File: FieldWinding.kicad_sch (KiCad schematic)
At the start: 39 parts, among them J9 Conn_02x10_Odd_Even, U27 ADM3485, U29 ADM3485, U30 ADM3485, U67 ADM3485, U72 LMV321

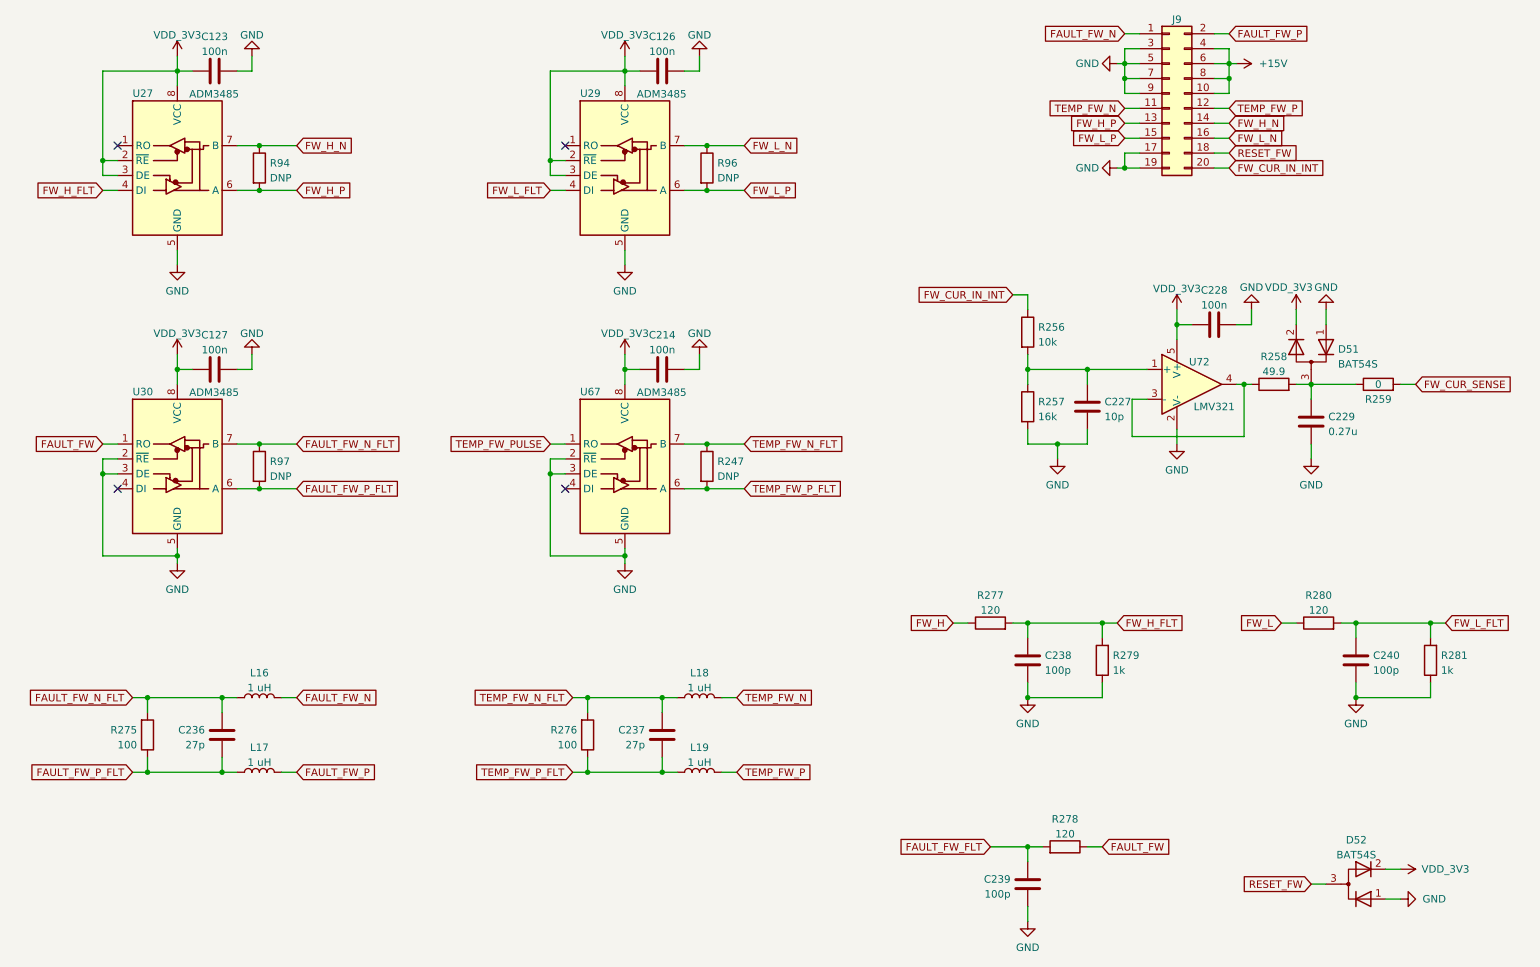
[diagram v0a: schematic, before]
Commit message: Изменения в схеме: убрал разъемы датчиков тока
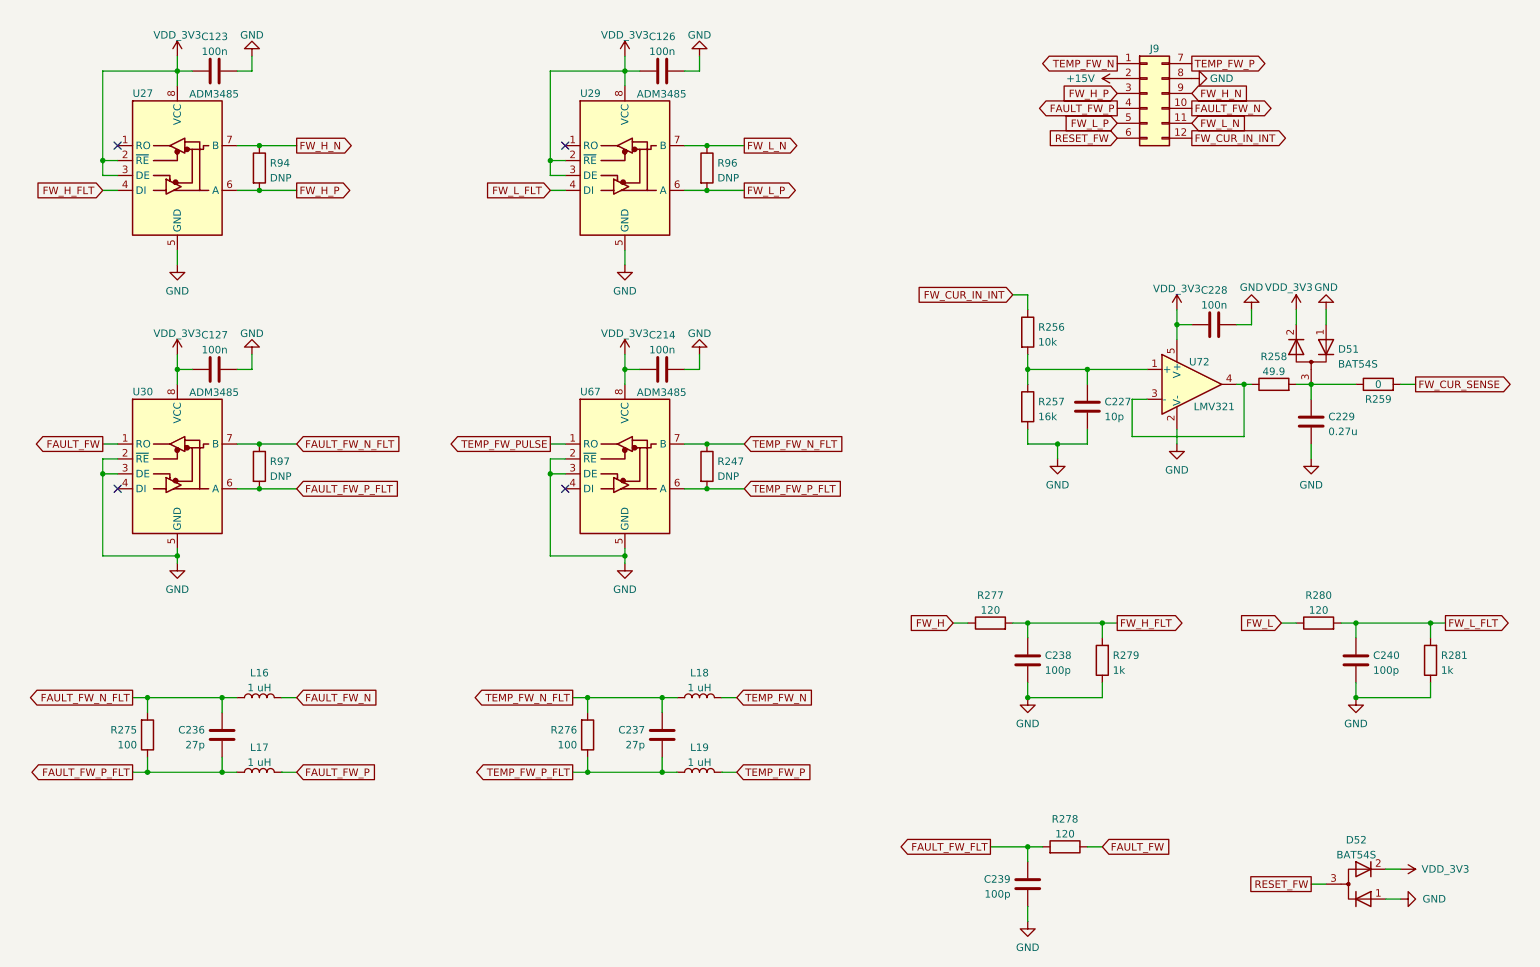
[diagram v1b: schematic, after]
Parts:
- removed J9: Conn_02x10_Odd_Even, Project_Library:2-338069-0, symbol Connector_Generic:Conn_02x10_Odd_Even
- added J9: ~, Connector_Molex:Molex_Micro-Fit_3.0_43045-1200_2x06_P3.00mm_Horizontal, symbol Connector_Generic:Conn_02x06_Top_Bottom
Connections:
- net +15V: now also J9.2 (Pin_2)
- net FAULT_FW_N: now also J9.10 (Pin_10)
- net FAULT_FW_P: now also J9.4 (Pin_4)
- net FW_CUR_IN_INT: now also J9.12 (Pin_12)
- net FW_H_N: now also J9.9 (Pin_9)
- net FW_H_P: now also J9.3 (Pin_3)
- net FW_L_N: now also J9.11 (Pin_11)
- net FW_L_P: now also J9.5 (Pin_5)
- net GND: now also J9.8 (Pin_8)
- net RESET_FW: now also J9.6 (Pin_6)
- net TEMP_FW_N: now also J9.1 (Pin_1)
- net TEMP_FW_P: now also J9.7 (Pin_7)

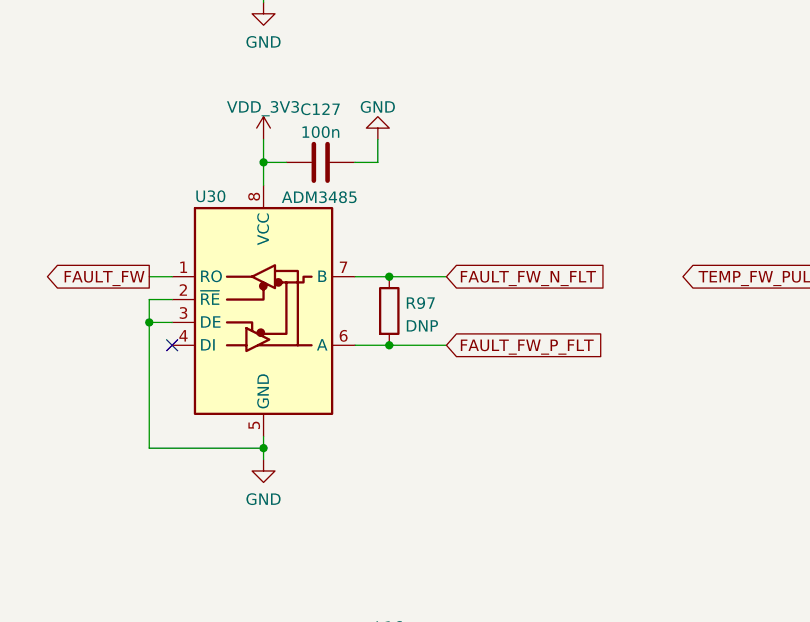
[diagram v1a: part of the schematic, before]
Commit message: Изменения: добавил 3или для фолтов трёхфазного модуля
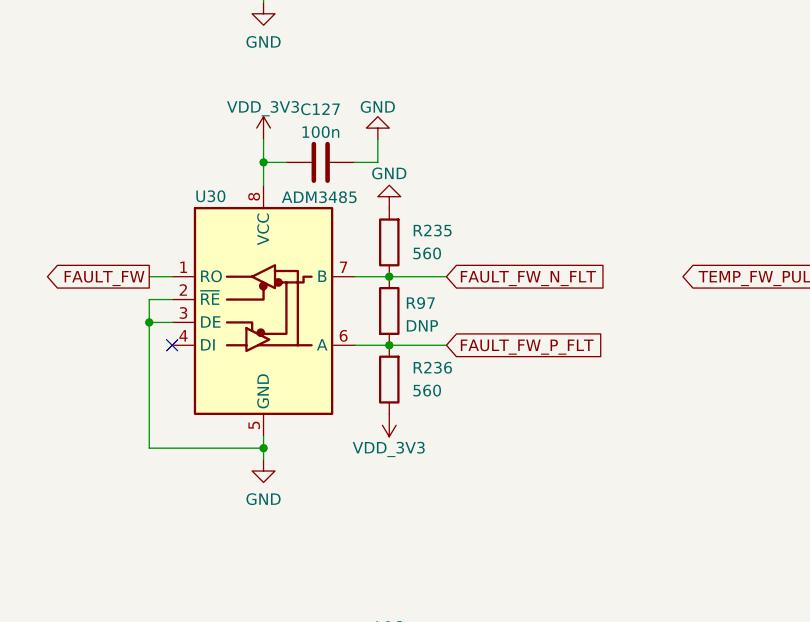
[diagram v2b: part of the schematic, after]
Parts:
- added R235, R236: 560, Resistor_SMD:R_0603_1608Metric, symbol Device:R
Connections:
- net FAULT_FW_N_FLT: now also R235.1
- net FAULT_FW_P_FLT: now also R236.2
- net GND: now also R235.2
- net VDD_3V3: now also R236.1

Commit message: REV_C: добавил Э3
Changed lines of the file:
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@@
 (kicad_sch
-	(version 20231120)
+	(version 20250114)
 	(generator "eeschema")
-	(generator_version "8.0")
+	(generator_version "9.0")
 	(paper "A4")
+	(title_block
+		(comment 1 "НВЦТ.EVP150-2-1.3000.100 Э3")
+	)
 	(junction
 		(at 121.92 101.6)
